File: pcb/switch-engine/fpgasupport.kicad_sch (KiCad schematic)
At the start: 57 parts, among them J7 JUMPER_0402, J8 XILINX_JTAG, U10 74LVC1T45, U11 74LVC1T45, U12 74LVC1T45, U13 MT25QU256ABA8E12-0AUT, U8 XILINX_ULTRASCALEPLUS_B676

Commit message: First iteration of main board PCB schematic is now passing ERC
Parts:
- U8: value XILINX_ULTRASCALEPLUS_B676 -> XCKU5P-2FFVB676I
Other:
- note added: "FPGA boot/debug"
- note added: "FPGA control signal level shifting"
- note added: "FPGA decoupling"
- note added: "FPGA power"
- note added: "Flash"
- note added: "TODO: verify sufficient caps"
- note removed: "This assumes all HDIO at 3.3 and HPIO at 1.8 TODO verify"
- company: (none) -> Antikernel Labs
- title: (none) -> LATENTRED Ethernet Switch - Main Board
- moved on the sheet: C58, C59, C60, C61, C62, C63, C64, C65, C66, C67, C68, C69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

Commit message: Finished schematic review
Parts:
- added C102, C154, C155: 10 uF, azonenberg_pcb:EIA_0805_CAP_NOSILK, symbol device:C
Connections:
- net 1V8: now also U10.6 (VCCB), C102.1, C154.1; no longer U10.1 (VCCA), U10.5 (DIR)
- net 3V3: now also U10.1 (VCCA), C155.1; no longer U10.6 (VCCB)
- net FPGA_INIT: now also U10.4 (B); no longer U10.3 (A)
- net FPGA_INIT_3V3: now also U10.3 (A); no longer U10.4 (B)
- net GND: now also C102.2, C154.2, C155.2
- new net FPGA_INIT_OE: U10.5 (DIR)
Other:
- note removed: "TODO: verify sufficient caps"

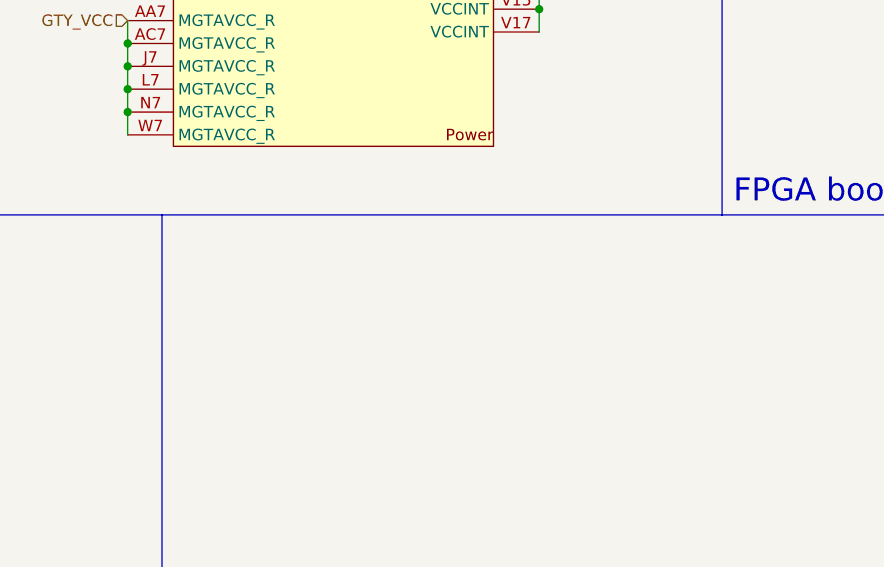
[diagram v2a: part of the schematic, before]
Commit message: Added footprints and created initial skeleton of layout
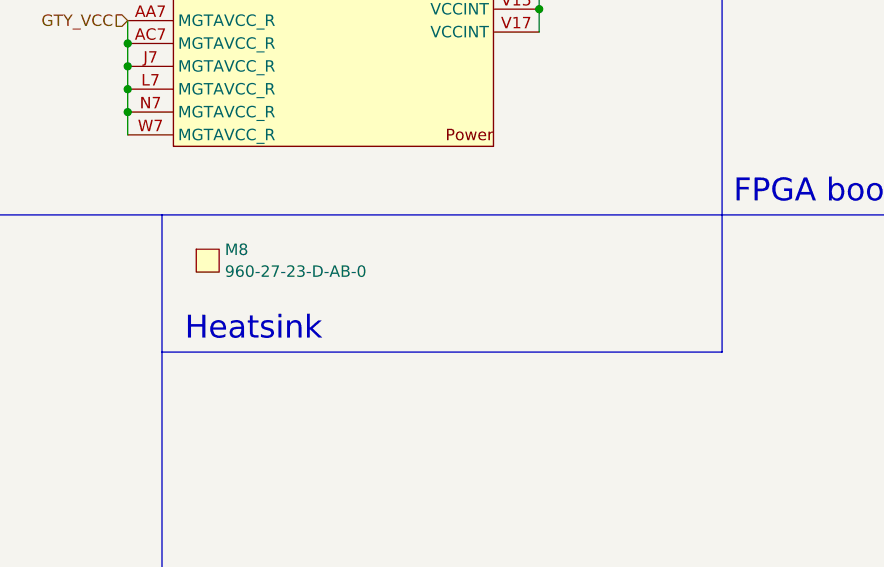
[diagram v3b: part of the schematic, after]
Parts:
- added M8: 960-27-23-D-AB-0, azonenberg_pcb:HEATSINK_WAKEFIELDVETTE_960-27-12-D-AB-0, symbol special-azonenberg:MECHANICAL
- U8: footprint (none) -> azonenberg_pcb:BGA_676_27x27_FULLARRAY_1MM_FFG676
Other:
- note added: "Heatsink"
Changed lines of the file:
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@@
 		)
 	)
+	(polyline
+		(pts
+			(xy 227.33 163.83) (xy 227.33 179.07)
+		)
+		(stroke
+			(width 0)
+			(type default)
+		)
+	)
 	(wire
 		(pts
@@
 		)
 	)
+	(polyline
+		(pts
+			(xy 165.1 179.07) (xy 227.33 179.07)
+		)
+		(stroke
+			(width 0)
+			(type default)
+		)
+	)
 	(wire
 		(pts
@@
 		)
 	)
+	(text "Heatsink"
+		(exclude_from_sim no)
+		(at 167.64 176.53 0)
+		(effects
+			(font
+				(size 2.54 2.54)
+			)
+			(justify left)
+		)
+	)
 	(text "VCCAUX"
 		(exclude_from_sim no)
@@
 			)
 		)
-		(property "Footprint" ""
+		(property "Footprint" "azonenberg_pcb:BGA_676_27x27_FULLARRAY_1MM_FFG676"
 			(at 356.87 92.71 0)
 			(effects
@@
 			)
 		)
-		(property "Footprint" ""
+		(property "Footprint" "azonenberg_pcb:BGA_676_27x27_FULLARRAY_1MM_FFG676"
 			(at 88.9 154.94 0)
 			(effects
@@
 			)
 		)
-		(property "Footprint" ""
+		(property "Footprint" "azonenberg_pcb:BGA_676_27x27_FULLARRAY_1MM_FFG676"
 			(at 154.94 154.94 0)
 			(effects
@@
 			)
 		)
-		(property "Footprint" ""
+		(property "Footprint" "azonenberg_pcb:BGA_676_27x27_FULLARRAY_1MM_FFG676"
 			(at 229.87 154.94 0)
 			(effects
@@
 					(unit 1)
 				)
+			)
+		)
+	)
+	(symbol
+		(lib_id "special-azonenberg:MECHANICAL")
+		(at 168.91 168.91 0)
+		(unit 1)
+		(exclude_from_sim no)
+		(in_bom yes)
+		(on_board yes)
+		(dnp no)
+		(fields_autoplaced yes)
+		(property "Reference" "M8"
+			(at 172.085 167.6978 0)
+			(effects
+				(font
+					(size 1.27 1.27)
+				)
+				(justify left)
+			)
+		)
+		(property "Value" "960-27-23-D-AB-0"
+			(at 172.085 170.1221 0)
+			(effects
+				(font
+					(size 1.27 1.27)
+				)
+				(justify left)
+			)
+		)
+		(property "Footprint" "azonenberg_pcb:HEATSINK_WAKEFIELDVETTE_960-27-12-D-AB-0"
+			(at 168.91 168.91 0)
+			(effects
+				(font
+					(size 1.27 1.27)
+				)
+				(hide yes)
+			)
+		)
+		(property "Datasheet" ""
+			(at 168.91 168.91 0)
+			(effects
+				(font
+					(size 1.27 1.27)
+				)
+				(hide yes)
+			)
+		)
+		(property "Description" ""
+			(at 168.91 168.91 0)
+			(effects
+				(font
+					(size 1.27 1.27)
+				)
+				(hide yes)
+			)
+		)
+		(instances
+			(project "switch-engine"
+				(path "/2594b26d-2fe5-4054-81d2-ca5df3747243/9989755c-0d3b-4905-8e52-92e034d7bb45"
+					(reference "M8")
+					(unit 1)
+				)

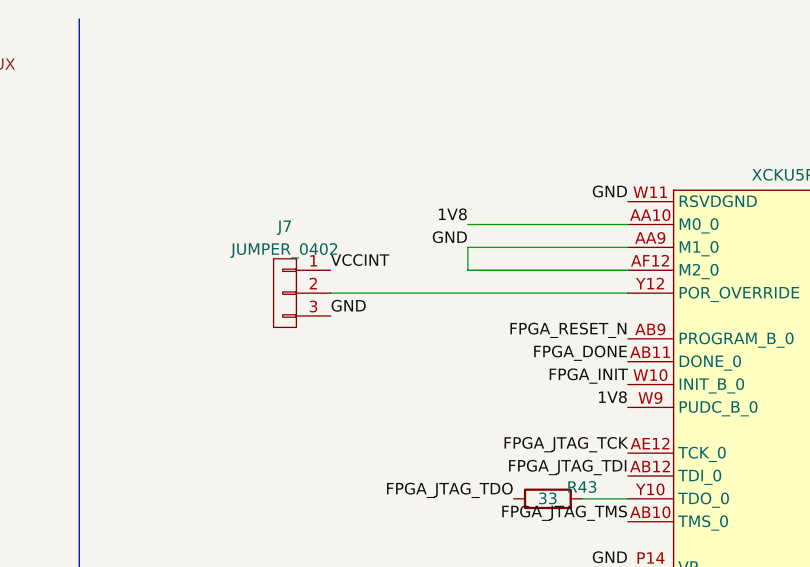
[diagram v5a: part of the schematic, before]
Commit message: Continued routing main MCU and FPGA support parts, hooked up part of boot flash
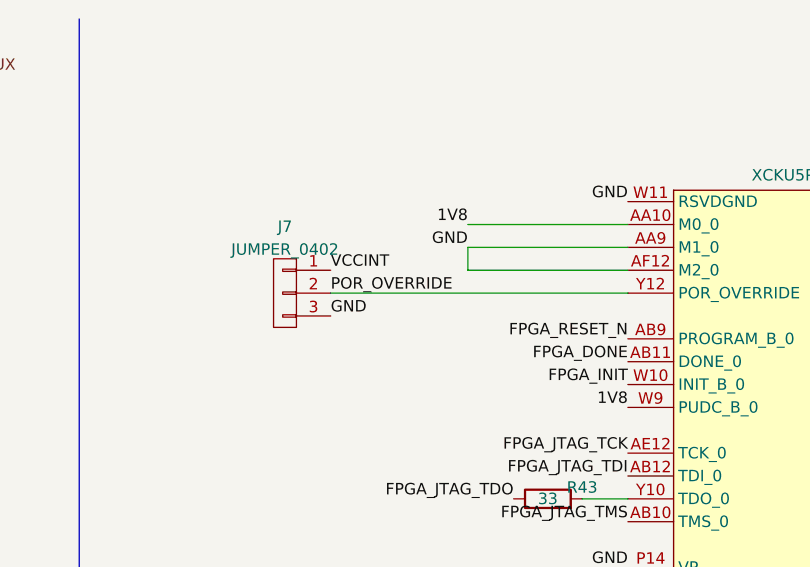
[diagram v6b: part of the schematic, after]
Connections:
- net POR_OVERRIDE: now reaches J7.2 (P2), U8.Y12 (POR_OVERRIDE)
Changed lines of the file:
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@@
 	(title_block
 		(title "LATENTRED Ethernet Switch - Main Board")
-		(date "2025-06-06")
+		(date "2025-06-07")
 		(rev "0.1")
 		(company "Antikernel Labs")
@@
 		)
 	)
+	(label "POR_OVERRIDE"
+		(at 255.27 44.45 0)
+		(fields_autoplaced yes)
+		(effects
+			(font
+				(size 1.27 1.27)
+			)
+			(justify left bottom)
+		)
+	)
